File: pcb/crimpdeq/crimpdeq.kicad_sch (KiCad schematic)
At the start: 50 parts, among them J2 USB4105-GF-A, Q1 SS8550, Q2 DMG3415U, U1 ESP32-C3-MINI-1, U2 MCP73831T-2ACI/OT, U3 HX711, U4 Rust_Board, U5 MAX17048G+T10, U6 SY8088

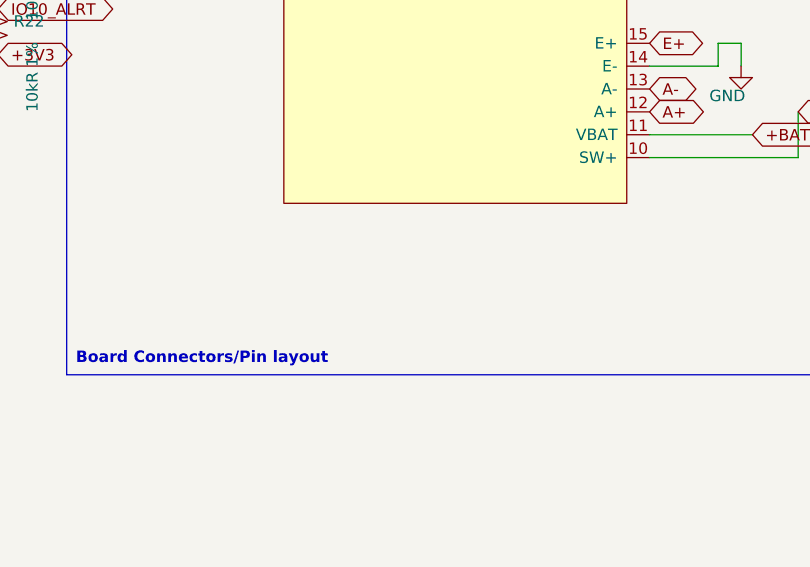
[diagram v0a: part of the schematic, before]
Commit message: feat: split cable pads into independent battery and sense points
Replace the shared J4 multi-pad header with separate THT pads so B+/B-,
SW+/SW-, and A+/A- can be wired independently, and place the battery
column clear of USB/power copper.

Co-authored-by: Cursor <cursoragent@cursor.com>
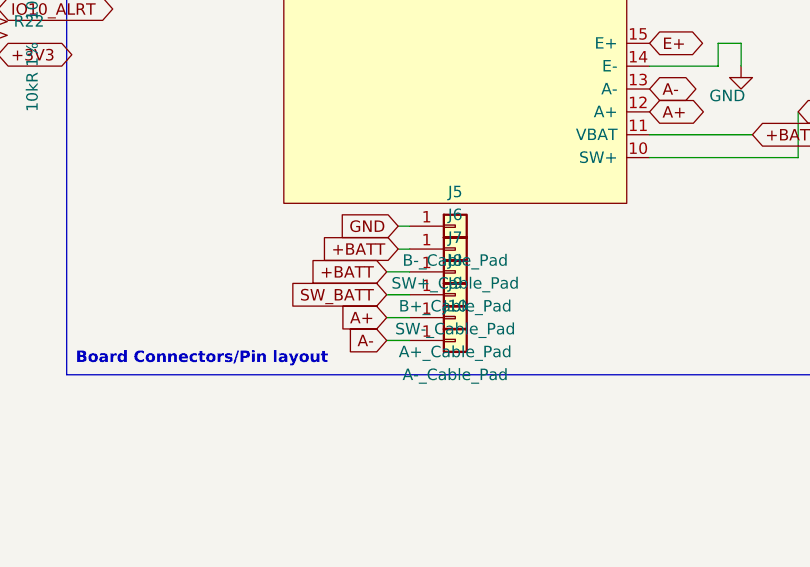
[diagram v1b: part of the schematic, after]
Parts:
- added J10: A-_Cable_Pad, TestPoint:TestPoint_THTPad_D1.5mm_Drill0.7mm, symbol Connector_Generic:Conn_01x01
- added J5: B-_Cable_Pad, TestPoint:TestPoint_THTPad_D1.5mm_Drill0.7mm, symbol Connector_Generic:Conn_01x01
- added J6: SW+_Cable_Pad, TestPoint:TestPoint_THTPad_D1.5mm_Drill0.7mm, symbol Connector_Generic:Conn_01x01
- added J7: B+_Cable_Pad, TestPoint:TestPoint_THTPad_D1.5mm_Drill0.7mm, symbol Connector_Generic:Conn_01x01
- added J8: SW-_Cable_Pad, TestPoint:TestPoint_THTPad_D1.5mm_Drill0.7mm, symbol Connector_Generic:Conn_01x01
- added J9: A+_Cable_Pad, TestPoint:TestPoint_THTPad_D1.5mm_Drill0.7mm, symbol Connector_Generic:Conn_01x01
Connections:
- net +BATT: now also J6.1 (Pin_1), J7.1 (Pin_1)
- net A+: now also J9.1 (Pin_1)
- net A-: now also J10.1 (Pin_1)
- net GND: now also J5.1 (Pin_1)
- net SW_BATT: now also J8.1 (Pin_1)

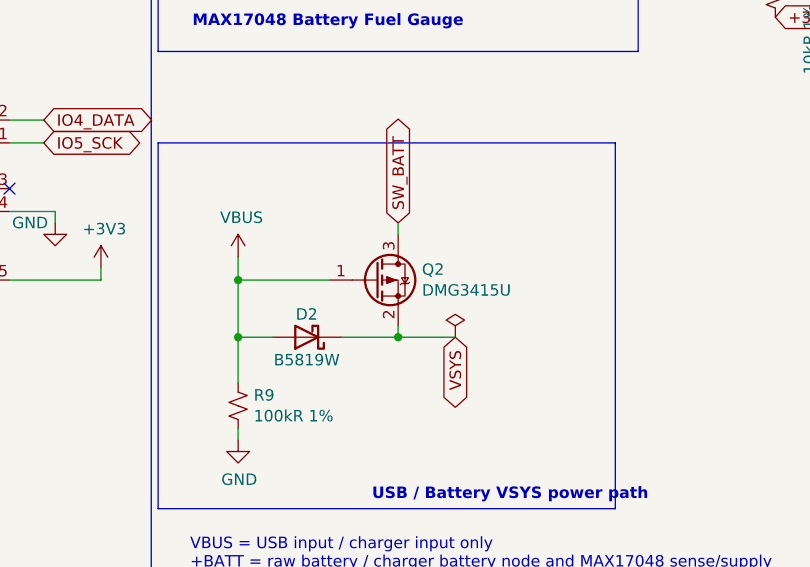
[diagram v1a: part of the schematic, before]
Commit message: fix: clean up cable-pad silk, Q2 symbol, and verification golden
Align the board with the post-split review: correct silk and shell vias,
use a pin-compatible PMOS symbol for DMG3415U, and update BOM/CPL/verify
for independent J5–J10 pads.

Co-authored-by: Cursor <cursoragent@cursor.com>
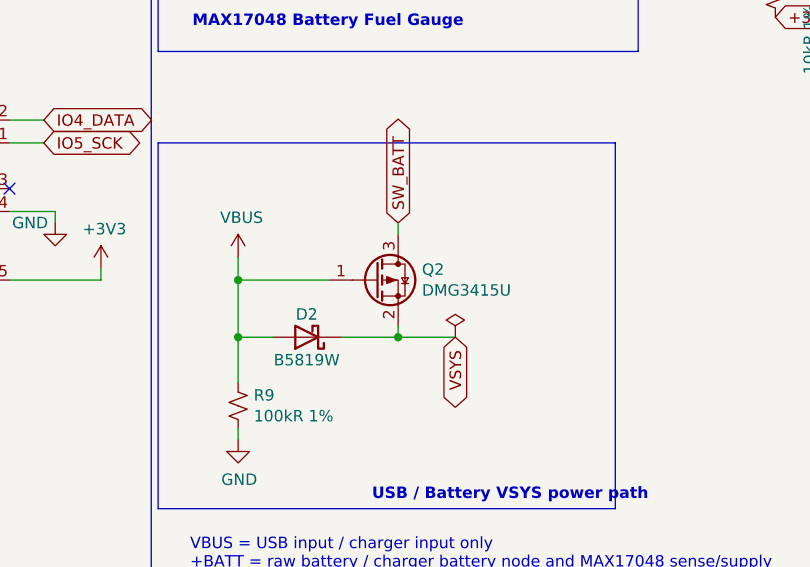
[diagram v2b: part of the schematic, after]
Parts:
- Q2: symbol Transistor_FET:DMG2301L -> Transistor_FET:Q_PMOS_GSD
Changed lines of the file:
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@@
           (unit 1)))))
   (symbol
-    (lib_id "Transistor_FET:DMG2301L")
+    (lib_id "Transistor_FET:Q_PMOS_GSD")
     (at 146.05 153.67 0)
     (unit 1)
@@
           (italic yes))
         (justify left)))
-    (property "Datasheet" "https://www.diodes.com/assets/Datasheets/DMG2301L.pdf"
+    (property "Datasheet" "https://www.diodes.com/assets/Datasheets/ds31785.pdf"
       (at 146.05 153.67 0)
       (hide yes)
@@
         (font
           (size 1.27 1.27))))
-    (property "Datasheet" ""
+    (property "Datasheet" "https://datasheets.maximintegrated.com/en/ds/MAX17048-MAX17049.pdf"
       (at 149.86 111.76 0)
       (hide yes)

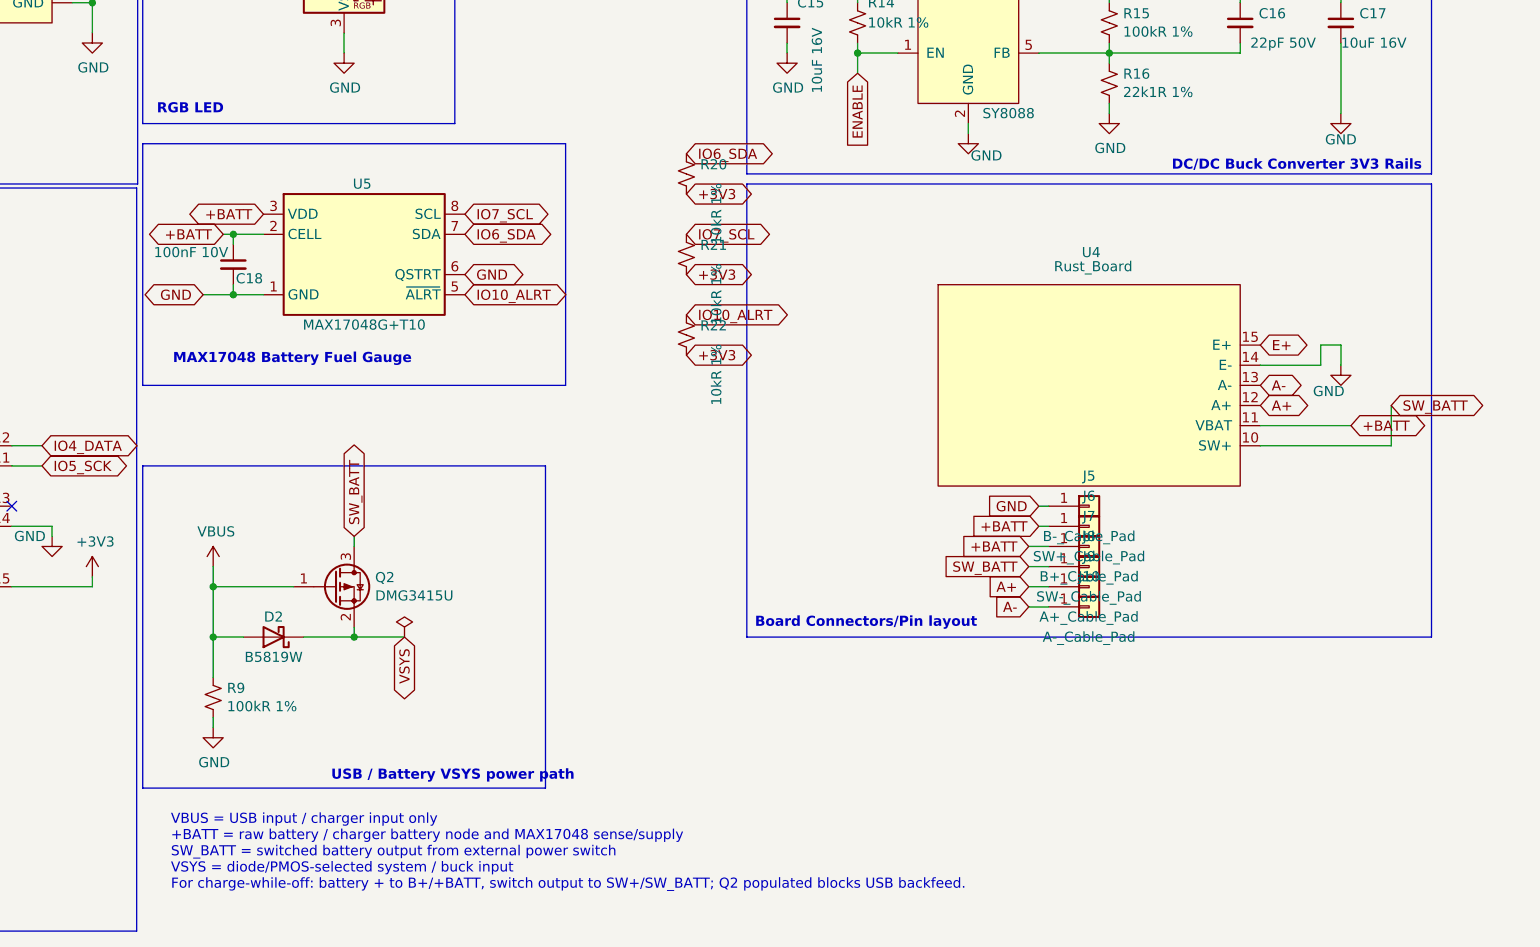
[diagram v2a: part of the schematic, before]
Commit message: feat: replace J3/U4 with independent E+ and E- cable pads
Make excitation pads match the other single-pad connectors, drop the
board-only J3 footprint and U4 harness symbol, and refresh schematic
layout plus verification/assembly artifacts.

Co-authored-by: Cursor <cursoragent@cursor.com>
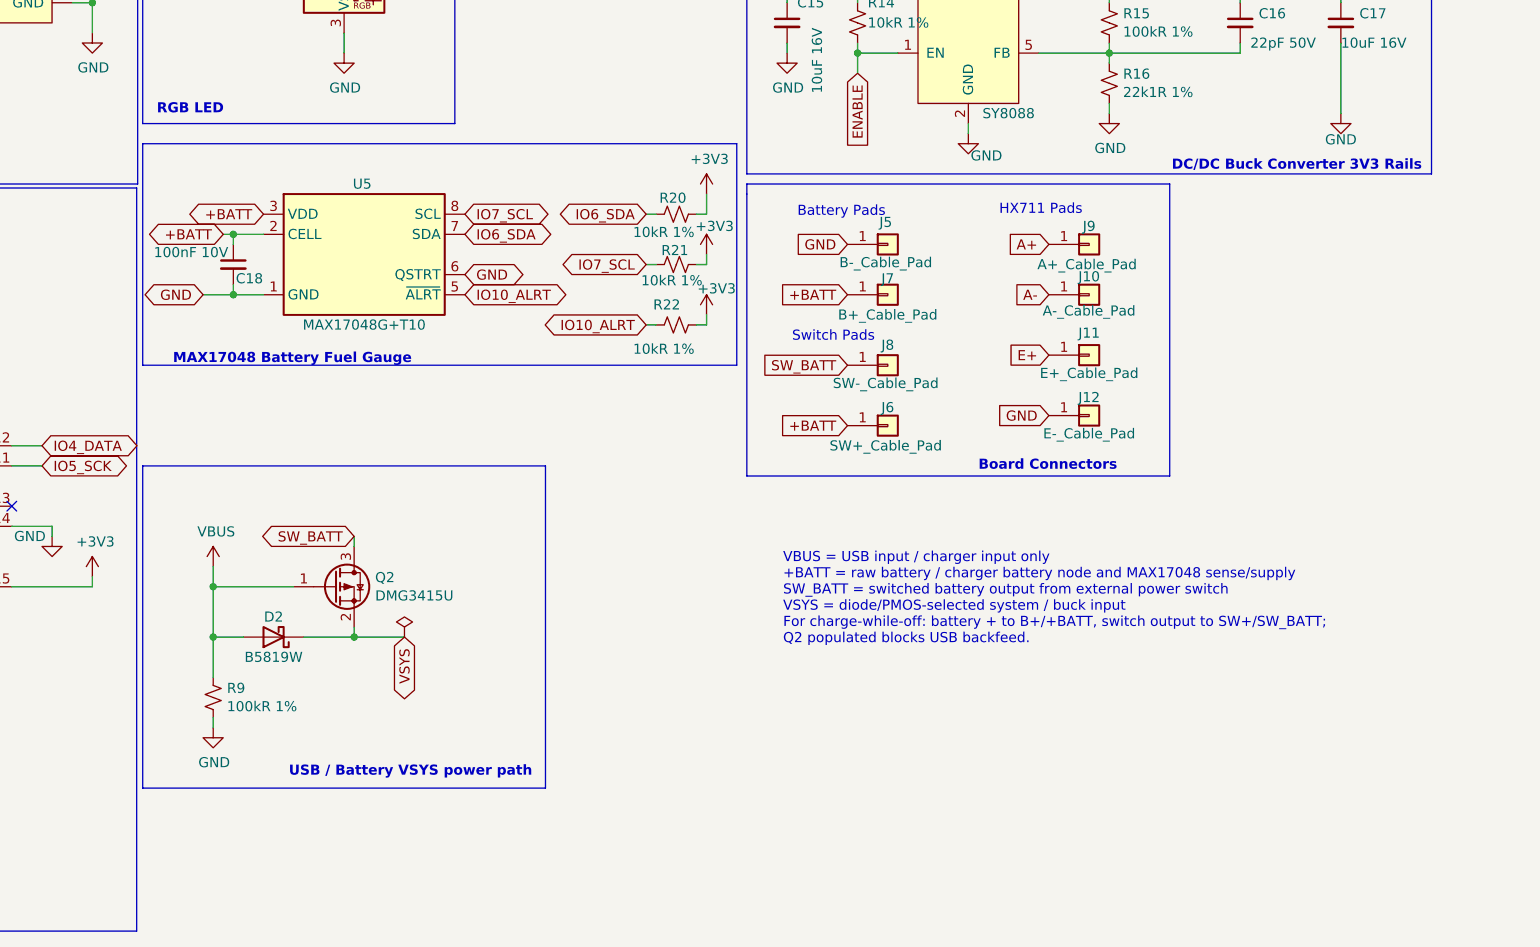
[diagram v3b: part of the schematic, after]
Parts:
- removed U4: Rust_Board, symbol Rust_Board:Rust_Board
- added J11: E+_Cable_Pad, TestPoint:TestPoint_THTPad_D1.5mm_Drill0.7mm, symbol Connector_Generic:Conn_01x01
- added J12: E-_Cable_Pad, TestPoint:TestPoint_THTPad_D1.5mm_Drill0.7mm, symbol Connector_Generic:Conn_01x01
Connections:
- net E+: now also J11.1 (Pin_1)
- net GND: now also J12.1 (Pin_1)
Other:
- note added: "Battery Pads"
- note added: "Board Connectors"
- note added: "HX711 Pads"
- note added: "Switch Pads"
- note removed: "Board Connectors/Pin layout"
- moved on the sheet: J10, J5, J6, J7, J8, J9, R20, R21, R22

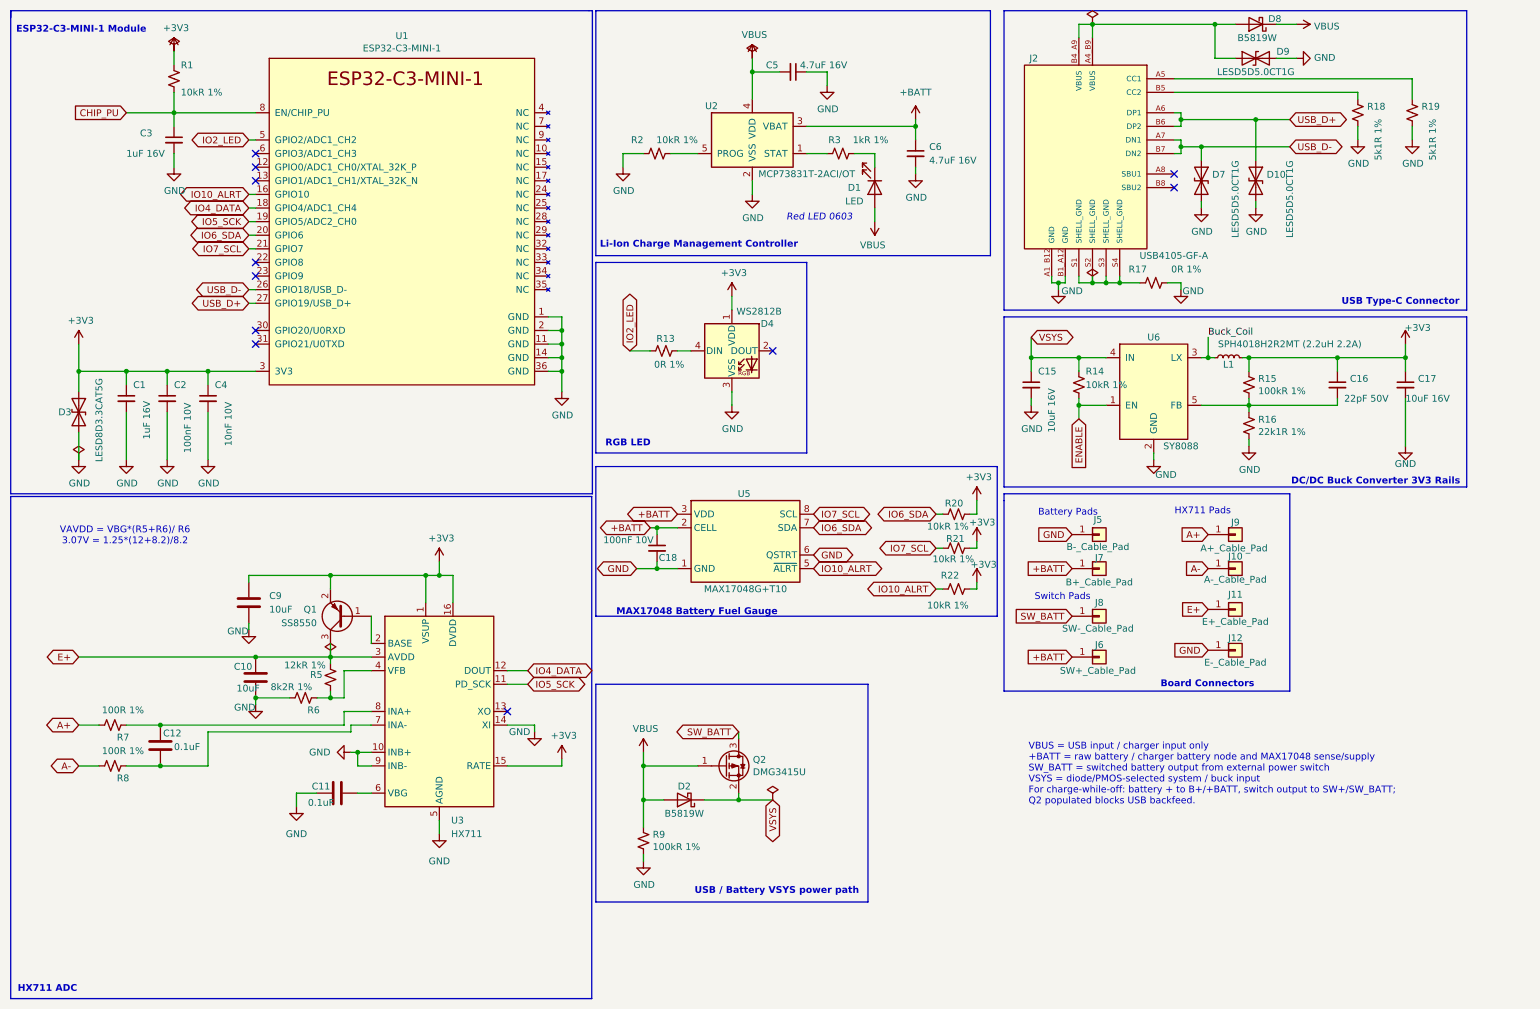
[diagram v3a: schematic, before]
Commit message: feat: replace HX711 with ADS1220 ratiometric front-end
Swap U3 to ADS1220 TSSOP-16 with +3V3 excitation and 4-wire SPI, drop the
HX711 bias network, and document on-demand Freerouting instead of vendoring JREs.

Co-authored-by: Cursor <cursoragent@cursor.com>
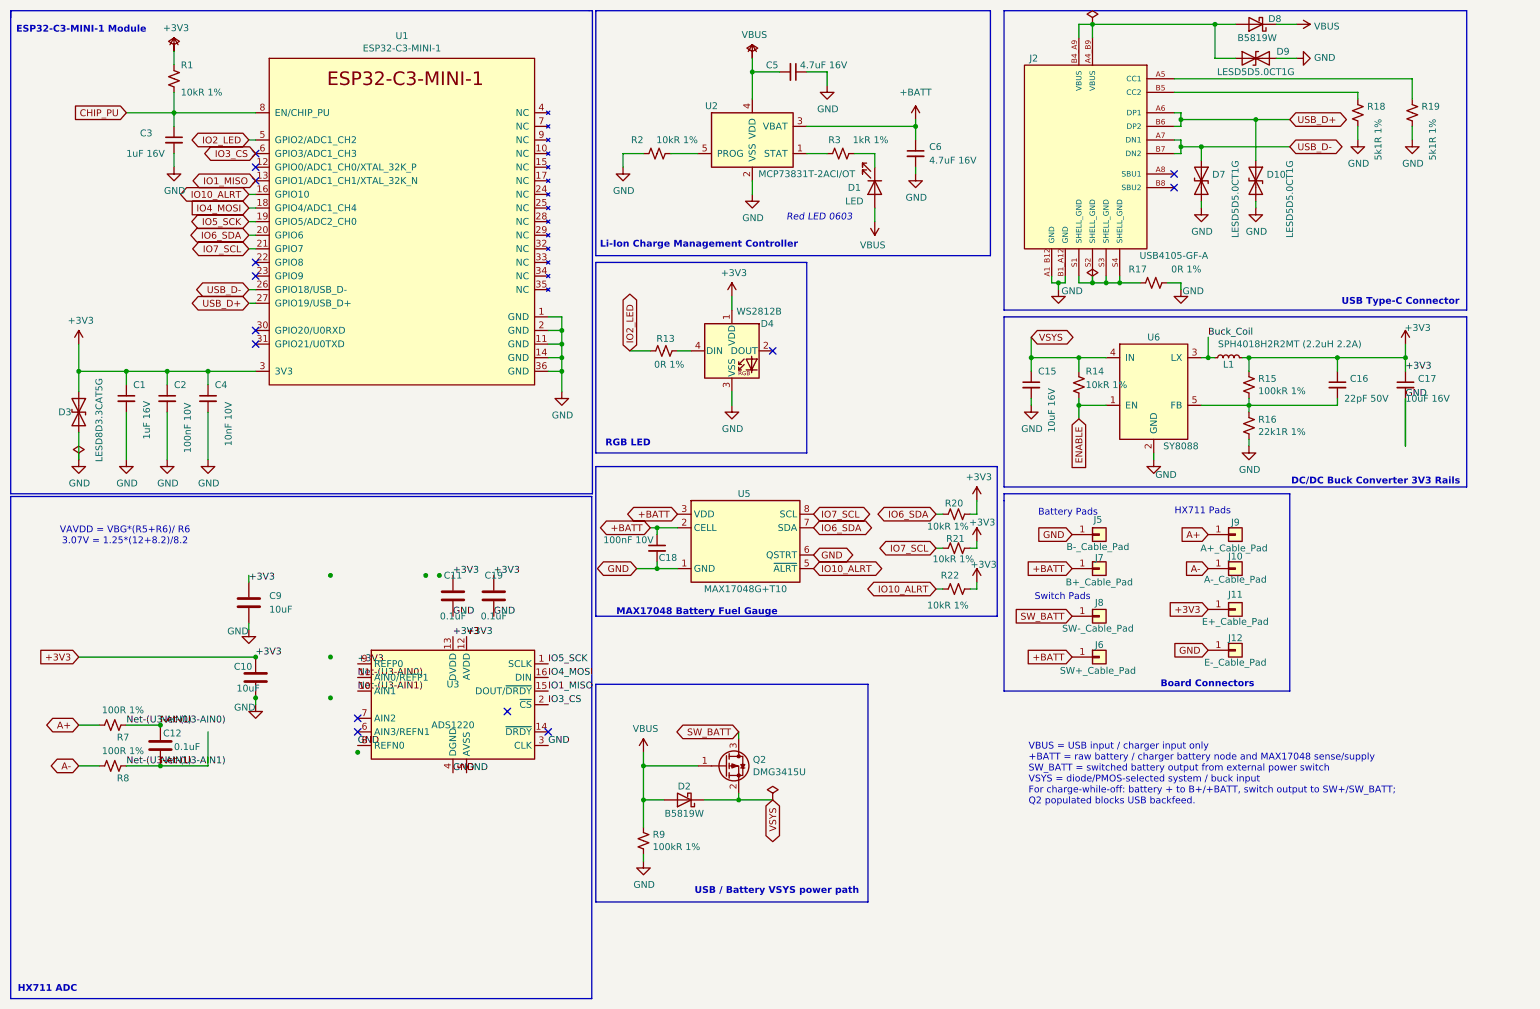
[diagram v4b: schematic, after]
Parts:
- removed Q1: SS8550, Package_TO_SOT_SMD:SOT-23, symbol Transistor_BJT:SS8550
- removed R5: 12kR 1%, Resistor_SMD:R_0402_1005Metric, symbol Device:R_Small_US
- removed R6: 8k2R 1%, Resistor_SMD:R_0402_1005Metric, symbol Device:R_Small_US
- removed U3: HX711, Package_SO:SOP-16_3.9x9.9mm_P1.27mm, symbol Analog_ADC:HX711
- added C19: 0.1uF, Capacitor_SMD:C_0603_1608Metric, symbol Device:C
- added U3: ADS1220, Package_SO:TSSOP-16_4.4x5mm_P0.65mm, symbol Analog_ADC:ADS1220xPW
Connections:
- net E+ is gone; now on net +3V3: C10.1, J11.1 (Pin_1)
- net +3V3: now also C11.1, C19.1, U3.12 (AVDD), U3.13 (DVDD), U3.9 (REFP0)
- net GND: now also C11.2, C19.2, U3.3 (CLK), U3.4 (DGND), U3.5 (AVSS), U3.8 (REFN0); no longer C11.1
- net IO5_SCK: now also U3.1 (SCLK)
- net Net-(U3-AIN0): now reaches C12.1, R7.1
- net Net-(U3-AIN0): now also U3.11 (AIN0/REFP1)
- net Net-(U3-AIN1): now reaches C12.2, R8.1
- net Net-(U3-AIN1): now also U3.10 (AIN1)
- net IO1_MISO: now reaches U1.13 (GPIO1/ADC1_CH1/XTAL_32K_N)
- net IO1_MISO: now also U3.15 (DOUT/~{DRDY})
- net IO3_CS: now reaches U1.6 (GPIO3/ADC1_CH3)
- net IO3_CS: now also U3.2 (~{CS})
- net IO4_DATA renamed IO4_MOSI
- net IO4_MOSI: now also U3.16 (DIN)
- no-connect marks 11 -> 14
